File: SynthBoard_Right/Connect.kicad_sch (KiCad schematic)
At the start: 3 parts, among them J1 DigiInput, J2 InLFO OutEnv, J8 VCFOut

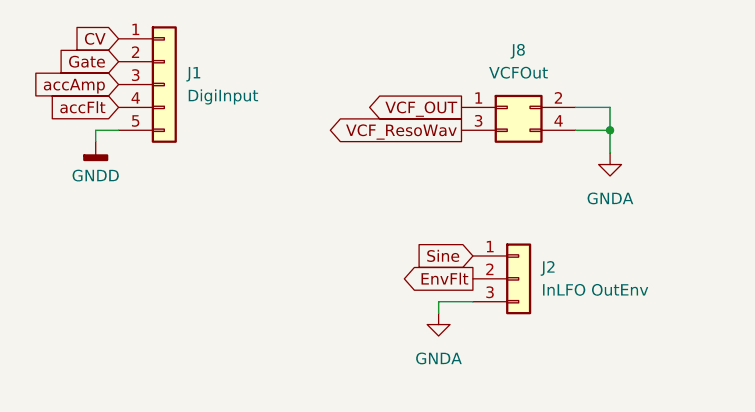
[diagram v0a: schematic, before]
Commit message: SynthBoard Right
配線ミスを修正
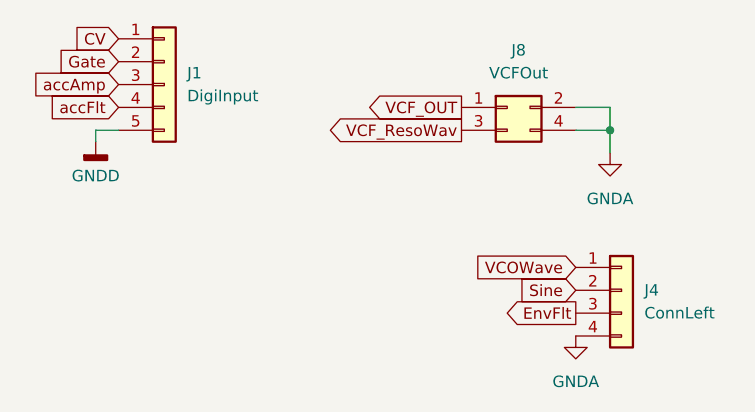
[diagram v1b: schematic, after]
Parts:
- removed J2: InLFO OutEnv, Connector_PinSocket_2.54mm:PinSocket_1x03_P2.54mm_Vertical, symbol Connector_Generic:Conn_01x03
- added J4: ConnLeft, Connector_PinSocket_2.54mm:PinSocket_1x04_P2.54mm_Vertical, symbol Connector_Generic:Conn_01x04
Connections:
- net EnvFlt: now also J4.3 (Pin_3)
- net GNDA: now also J4.4 (Pin_4)
- net Sine: now also J4.2 (Pin_2)
- new net VCOWave: J4.1 (Pin_1)
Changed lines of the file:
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@@
 	(wire
 		(pts
-			(xy 153.67 97.79) (xy 149.86 97.79)
+			(xy 168.91 76.2) (xy 168.91 78.74)
 		)
 		(stroke
@@
 	(wire
 		(pts
-			(xy 168.91 76.2) (xy 168.91 78.74)
+			(xy 114.3 78.74) (xy 111.76 78.74)
 		)
 		(stroke
@@
 	(wire
 		(pts
-			(xy 149.86 97.79) (xy 149.86 99.06)
+			(xy 111.76 78.74) (xy 111.76 80.01)
 		)
 		(stroke
@@
 		)
 	)
-	(wire
-		(pts
-			(xy 114.3 78.74) (xy 111.76 78.74)
-		)
-		(stroke
-			(width 0)
-			(type default)
-		)
-	)
-	(wire
-		(pts
-			(xy 111.76 78.74) (xy 111.76 80.01)
-		)
-		(stroke
-			(width 0)
-			(type default)
-		)
-	)
 	(global_label "EnvFlt"
 		(shape output)
-		(at 153.67 95.25 180)
-		(fields_autoplaced yes)
-		(effects
-			(font
-				(size 1.27 1.27)
-			)
-			(justify right)
-		)
-		(property "Intersheetrefs" "${INTERSHEET_REFS}"
-			(at 143.4883 95.25 0)
-			(effects
-				(font
-					(size 1.27 1.27)
-				)
-				(justify right)
-				(hide yes)
-			)
-		)
-	)
-	(global_label "Sine"
-		(shape input)
-		(at 153.67 92.71 180)
-		(fields_autoplaced yes)
-		(effects
-			(font
-				(size 1.27 1.27)
-			)
-			(justify right)
-		)
-		(property "Intersheetrefs" "${INTERSHEET_REFS}"
-			(at 146.6329 92.71 0)
+		(at 165.1 99.06 180)
+		(fields_autoplaced yes)
+		(effects
+			(font
+				(size 1.27 1.27)
+			)
+			(justify right)
+		)
+		(property "Intersheetrefs" "${INTERSHEET_REFS}"
+			(at 154.9183 99.06 0)
 			(effects
 				(font
@@
 		)
 	)
+	(global_label "VCOWave"
+		(shape input)
+		(at 165.1 93.98 180)
+		(fields_autoplaced yes)
+		(effects
+			(font
+				(size 1.27 1.27)
+			)
+			(justify right)
+		)
+		(property "Intersheetrefs" "${INTERSHEET_REFS}"
+			(at 153.7691 93.98 0)
+			(effects
+				(font
+					(size 1.27 1.27)
+				)
+				(justify right)
+				(hide yes)
+			)
+		)
+	)
 	(global_label "CV"
 		(shape input)
@@
 		)
 	)
+	(global_label "Sine"
+		(shape input)
+		(at 165.1 96.52 180)
+		(fields_autoplaced yes)
+		(effects
+			(font
+				(size 1.27 1.27)
+			)
+			(justify right)
+		)
+		(property "Intersheetrefs" "${INTERSHEET_REFS}"
+			(at 158.0629 96.52 0)
+			(effects
+				(font
+					(size 1.27 1.27)
+				)
+				(justify right)
+				(hide yes)
+			)
+		)
+	)
 	(symbol
-		(lib_id "Connector_Generic:Conn_01x03")
-		(at 158.75 95.25 0)
+		(lib_id "Connector_Generic:Conn_01x04")
+		(at 170.18 96.52 0)
 		(unit 1)
 		(exclude_from_sim no)
@@
 		(dnp no)
 		(fields_autoplaced yes)
-		(property "Reference" "J2"
-			(at 161.29 93.9799 0)
+		(property "Reference" "J4"
+			(at 172.72 96.5199 0)
 			(effects
 				(font
@@
 			)
 		)
-		(property "Value" "InLFO OutEnv"
-			(at 161.29 96.5199 0)
+		(property "Value" "ConnLeft"
+			(at 172.72 99.0599 0)
 			(effects
 				(font
@@
 			)
 		)
-		(property "Footprint" "Connector_PinSocket_2.54mm:PinSocket_1x03_P2.54mm_Vertical"
-			(at 158.75 95.25 0)
+		(property "Footprint" "Connector_PinSocket_2.54mm:PinSocket_1x04_P2.54mm_Vertical"
+			(at 170.18 96.52 0)
 			(effects
 				(font
@@
 		)
 		(property "Datasheet" "~"
-			(at 158.75 95.25 0)
-			(effects
-				(font
-					(size 1.27 1.27)
-				)
-				(hide yes)
-			)
-		)
-		(property "Description" "Generic connector, single row, 01x03, script generated (kicad-library-utils/schlib/autogen/connector/)"
-			(at 158.75 95.25 0)
-			(effects
-				(font
-					(size 1.27 1.27)
-				)
-				(hide yes)
-			)
+			(at 170.18 96.52 0)
+			(effects
+				(font
+					(size 1.27 1.27)
+				)
+				(hide yes)
+			)
+		)
+		(property "Description" "Generic connector, single row, 01x04, script generated (kicad-library-utils/schlib/autogen/connector/)"
+			(at 170.18 96.52 0)
+			(effects
+				(font
+					(size 1.27 1.27)
+				)
+				(hide yes)
+			)
+		)
+		(pin "3"
+		)
+		(pin "2"
 		)
 		(pin "1"
 		)
-		(pin "3"
-		)
-		(pin "2"
+		(pin "4"
 		)
 		(instances
 			(project ""
 				(path "/92765e2f-a998-485f-b610-76a9d5b50cba/a8184a09-2ac5-4159-bd95-783f5bee7b39"
-					(reference "J2")
+					(reference "J4")
 					(unit 1)
 				)
@@
 	(symbol
 		(lib_id "power:GNDA")
-		(at 149.86 99.06 0)
+		(at 165.1 101.6 0)
 		(unit 1)
 		(exclude_from_sim no)
@@
 		(fields_autoplaced yes)
 		(property "Reference" "#PWR01"
-			(at 149.86 105.41 0)
+			(at 165.1 107.95 0)
 			(effects
 				(font
@@
 		)
 		(property "Value" "GNDA"
-			(at 149.86 104.14 0)
+			(at 165.1 106.68 0)
 			(effects
 				(font
@@
 		)
 		(property "Footprint" ""
-			(at 149.86 99.06 0)
+			(at 165.1 101.6 0)
 			(effects
 				(font
@@
 		)
 		(property "Datasheet" ""
-			(at 149.86 99.06 0)
+			(at 165.1 101.6 0)
 			(effects
 				(font
@@
 		)
 		(property "Description" "Power symbol creates a global label with name \"GNDA\" , analog ground"
-			(at 149.86 99.06 0)
-			(effects
-				(font
+			(at 165.1 101.6 0)
+			(effects
+				(font
